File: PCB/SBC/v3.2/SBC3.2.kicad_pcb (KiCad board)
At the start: 2 copper layers, 127 x 96.5 mm, 73 parts, among them J1 ZTO-80 Bus, J10 Conn_01x02, J11 Conn_01x02, J2 Conn_01x02, J3 5V_IN, J4 CPUHDR, J5 CTCHDR, J6 SIOHDR, J7 PIOHDR, J8 PIOHDR, J9 SIOHDR, SW1 Reset, U1 Z80CPU, U2 Z80SIO0, U3 28C256, U4 Z80PIO, U5 AS6C62256, U6 Z80CTC, U7 74HC139, U8 ULN2803A, U9 74HC138, X1 SYS_CLK, X2 1.8432MHz

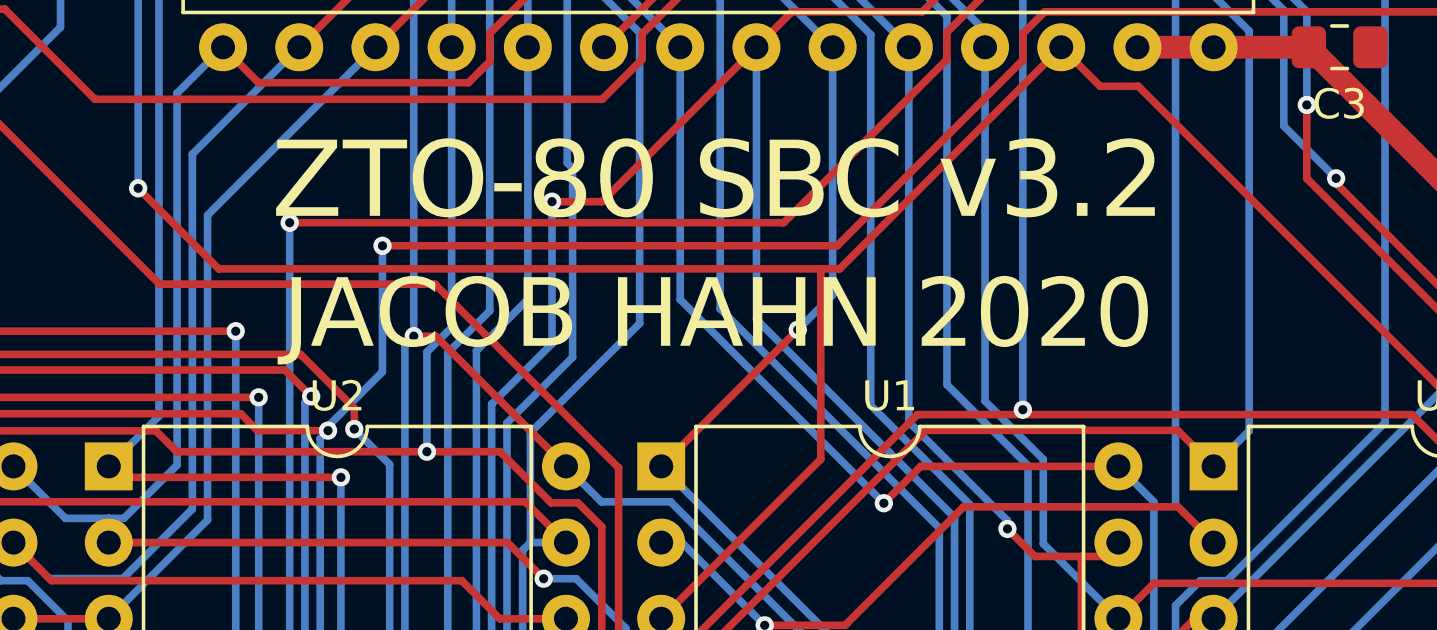
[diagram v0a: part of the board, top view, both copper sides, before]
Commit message: Changed SBC V3.2 files and added PDFs
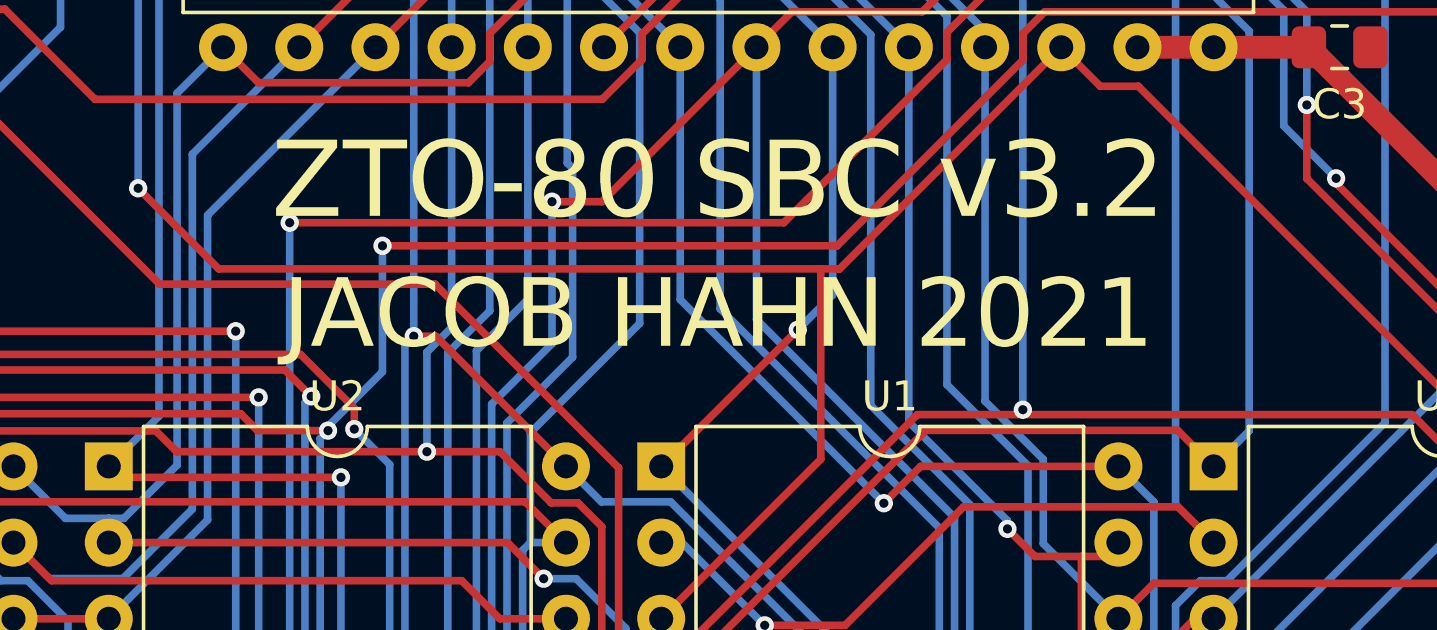
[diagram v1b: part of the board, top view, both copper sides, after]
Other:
- board text added: "JACOB HAHN 2021"
- board text removed: "JACOB HAHN 2020"
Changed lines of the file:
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@@
   (title_block
     (title "ZTO-80 SBC")
-    (date 2021-05-20)
+    (date 2021-09-26)
     (rev 3.2)
     (company "Jacob Hahn")
@@
       (drillshape 0)
       (scaleselection 1)
-      (outputdirectory "../../../../PCB/ZTO-80/Gerber/V3/"))
+      (outputdirectory "../../../../PCB/ZTO-80/Gerber/V3.2/"))
   )
   (net 0 "")
@@
     (effects (font (size 1.524 1.524) (thickness 0.254)))
   )
-  (gr_text "JACOB HAHN 2020" (at 146.05 93.98) (layer F.SilkS)
+  (gr_text "JACOB HAHN 2021" (at 146.05 93.98) (layer F.SilkS)
     (effects (font (size 2.286 2.286) (thickness 0.381)))
   )

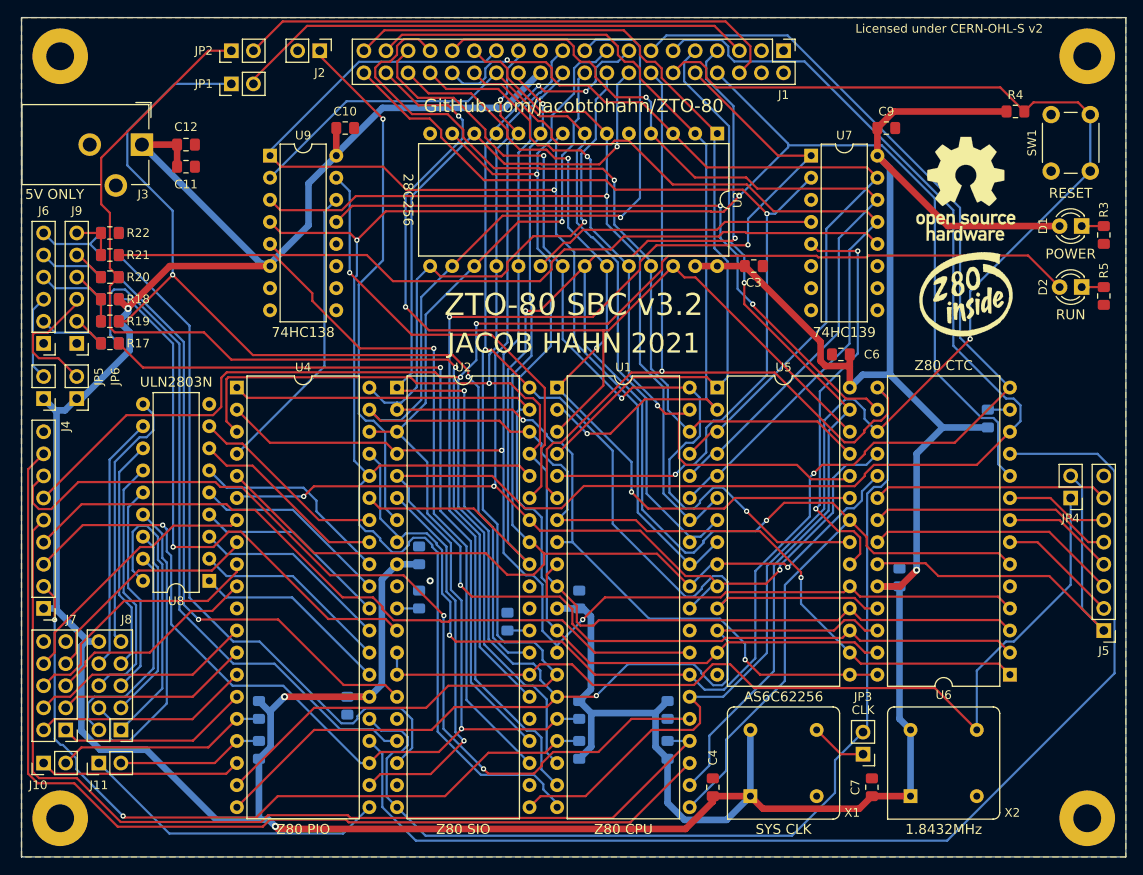
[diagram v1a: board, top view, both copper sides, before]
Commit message: Updates to 3.2 and SBC Backplane
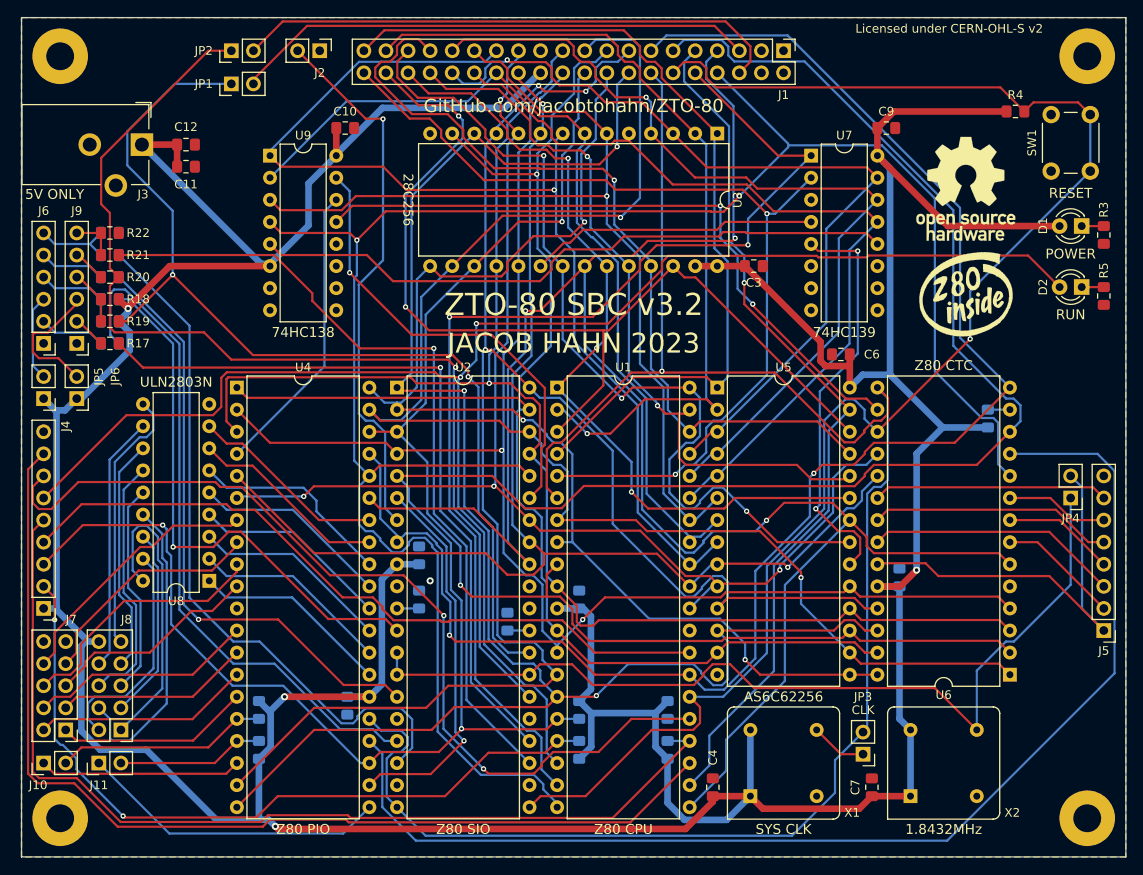
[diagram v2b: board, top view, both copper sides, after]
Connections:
- J2 pad 1: /EXIEI -> unconnected-(J2-Pad1)
- J2 pad 2: Net-(J2-Pad2) -> /EXIEI
- J7 pad 9: Net-(J7-Pad9) -> unconnected-(J7-Pad9)
- U2 pad 10: Net-(U2-Pad10) -> unconnected-(U2-Pad10)
- U2 pad 16: Net-(U2-Pad16) -> unconnected-(U2-Pad16)
- U2 pad 25: Net-(U2-Pad25) -> unconnected-(U2-Pad25)
- U2 pad 30: Net-(U2-Pad30) -> unconnected-(U2-Pad30)
- U7 pad 10: Net-(U7-Pad10) -> unconnected-(U7-Pad10)
- U7 pad 11: Net-(U7-Pad11) -> unconnected-(U7-Pad11)
- U7 pad 6: Net-(U7-Pad6) -> unconnected-(U7-Pad6)
- U7 pad 7: Net-(U7-Pad7) -> unconnected-(U7-Pad7)
- U7 pad 9: Net-(U7-Pad9) -> unconnected-(U7-Pad9)
- U9 pad 10: Net-(U9-Pad10) -> unconnected-(U9-Pad10)
- U9 pad 11: Net-(U9-Pad11) -> unconnected-(U9-Pad11)
- U9 pad 12: Net-(U9-Pad12) -> unconnected-(U9-Pad12)
- U9 pad 7: Net-(U9-Pad7) -> unconnected-(U9-Pad7)
- U9 pad 9: Net-(U9-Pad9) -> unconnected-(U9-Pad9)
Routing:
- net /EXIEI: track 60.5 -> 62.7 mm
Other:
- net class Default removed
- net class Power removed
- board text added: "JACOB HAHN 2023"
- board text removed: "JACOB HAHN 2021"
